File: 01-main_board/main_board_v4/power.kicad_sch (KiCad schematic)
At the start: 22 parts, among them IC1 MAX6105EUR+T, IC11 LT3973EMSE-5#PBF, IC2 LP5907MFX-2.5_NOPB, U4 TPS2115APWR

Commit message: regenerated gerbers
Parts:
- added R10: 100k, Resistor_SMD:R_0402_1005Metric, symbol Device:R_Small
- gave numbers to parts that had none: 1
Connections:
- net 5V_usb: now also R10.1; no longer R60.1
- net PGND: now also R10.2; no longer R60.2
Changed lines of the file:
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@@
 		(on_board yes)
 		(dnp no)
-		(property "Reference" "R?"
+		(property "Reference" "R10"
 			(at 122.936 118.872 0)
 			(effects
@@
 			(project "main_board_v4"
 				(path "/12c2237c-5932-49af-9119-92b28c846ae7/e4bc29b2-554a-4b47-958f-0b5bb716dd19"
-					(reference "R?")
+					(reference "R10")
 					(unit 1)
 				)
@@
 		(dnp no)
 		(fields_autoplaced yes)
-		(property "Reference" "#PWR?"
+		(property "Reference" "#PWR0101"
 			(at 132.08 111.76 0)
 			(effects
@@
 			(project "main_board_v4"
 				(path "/12c2237c-5932-49af-9119-92b28c846ae7/e4bc29b2-554a-4b47-958f-0b5bb716dd19"
-					(reference "#PWR?")
-					(unit 1)
-				)
+					(reference "#PWR0101")
+					(unit 1)
+				)

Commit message: Added tooling holes
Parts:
- IC11: footprint SOP50P490X110-11N -> (none)
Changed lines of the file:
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@@
 			)
 		)
-		(property "Footprint" "SOP50P490X110-11N"
+		(property "Footprint" ""
 			(at 76.2 195.25 0)
 			(effects

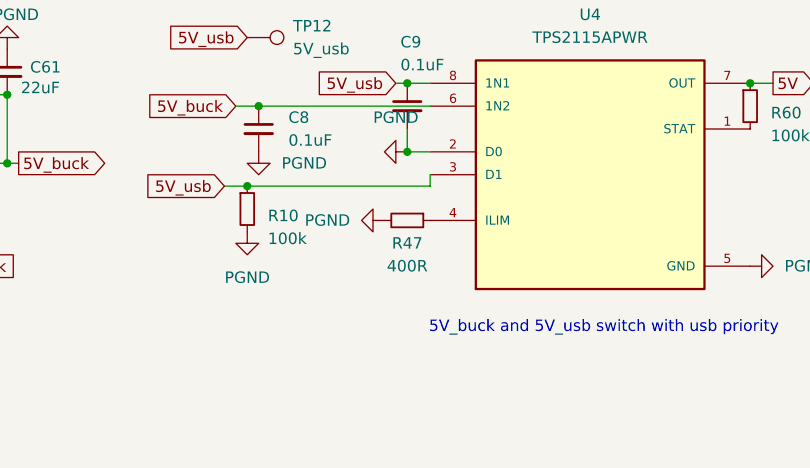
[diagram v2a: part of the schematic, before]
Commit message: Added comments and a resistor change
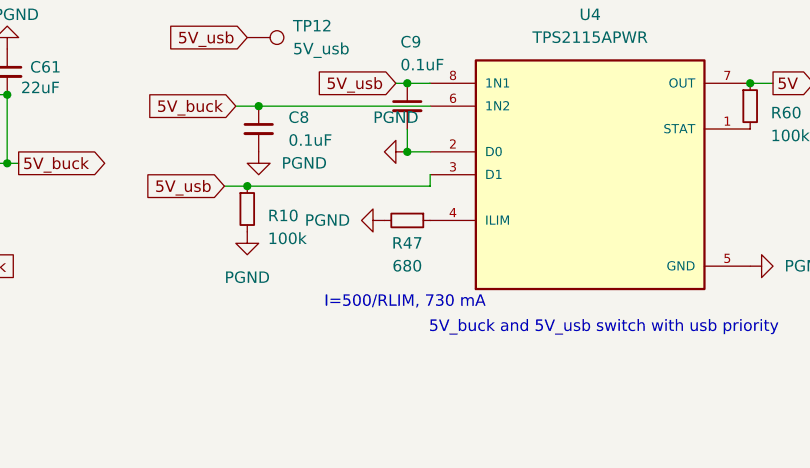
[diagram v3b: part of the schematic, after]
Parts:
- R47: value 400R -> 680
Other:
- note added: "I=500/RLIM, 730 mA"
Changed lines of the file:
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@@
 		)
 	)
+	(text "I=500/RLIM, 730 mA"
+		(exclude_from_sim no)
+		(at 138.176 128.524 0)
+		(effects
+			(font
+				(size 1.27 1.27)
+			)
+		)
+	)
 	(text "ESP32 recommends 3.3V power supply with >= 500 mA supply current, \n\nESP32C6 or ESP32S3 specifically, dobule check datasheets\n"
 		(exclude_from_sim no)
@@
 			)
 		)
-		(property "Value" "400R"
+		(property "Value" "680"
 			(at 138.43 124.46 90)
 			(effects
